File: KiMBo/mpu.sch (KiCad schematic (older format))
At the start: 11 parts, among them U1 OSD3358, U4 SN74AUC1G74DCTR

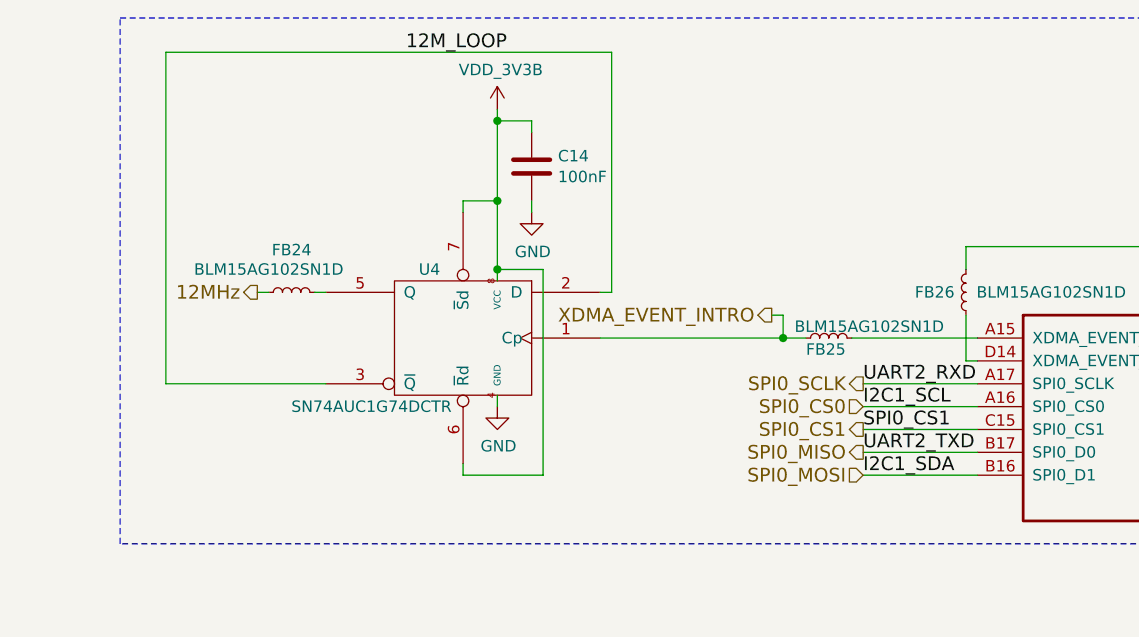
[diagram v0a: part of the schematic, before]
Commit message: Remove HDMI from the schematic
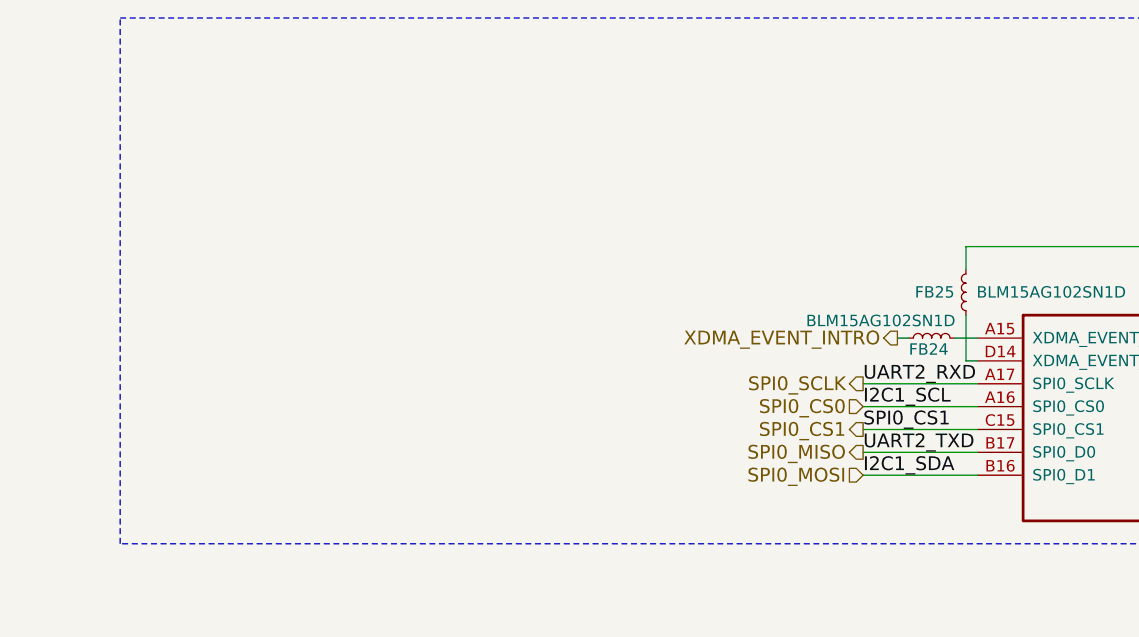
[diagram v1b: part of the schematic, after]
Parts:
- removed C14: 100nF, Capacitors_SMD:C_0603, symbol C
- removed FB24: BLM15AG102SN1D, Resistors_SMD:R_0402, symbol INDUCTOR_Small
- removed U4: SN74AUC1G74DCTR, KiMBo:DCT-MSOP-8_3x3mm_Pitch0.65mm, symbol 74LVC1G74
- renumbered FB25 to FB24, FB26 to FB25
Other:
- moved on the sheet: FB24
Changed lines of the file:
@@
 $Descr A3 16535 11693
 encoding utf-8
-Sheet 5 26
+Sheet 5 25
 Title ""
 Date ""
@@
 $EndComp
 $Comp
-L GND #PWR088
+L GND #PWR086
 U 1 1 584B7680
 P 6100 7850
-F 0 "#PWR088" H 6100 7600 50  0001 C CNN
+F 0 "#PWR086" H 6100 7600 50  0001 C CNN
 F 1 "GND" H 6105 7677 50  0000 C CNN
 F 2 "" H 6100 7850 50  0000 C CNN
@@
 	1    0    0    -1
 $EndComp
-$Comp
-L 74LVC1G74 U4
-U 1 1 584D5286
-P 6750 3850
-F 0 "U4" H 6850 4150 50  0000 L CNN
-F 1 "SN74AUC1G74DCTR" H 6800 3550 50  0000 L CNN
-F 2 "KiMBo:DCT-MSOP-8_3x3mm_Pitch0.65mm" H 6750 3850 50  0001 C CNN
-F 3 "" H 6750 3850 50  0000 C CNN
-	1    6750 3850
-	-1   0    0    -1
-$EndComp
-$Comp
-L GND #PWR089
-U 1 1 584D67FE
-P 6900 4150
-F 0 "#PWR089" H 6900 3900 50  0001 C CNN
-F 1 "GND" H 6905 3977 50  0000 C CNN
-F 2 "" H 6900 4150 50  0000 C CNN
-F 3 "" H 6900 4150 50  0000 C CNN
-	1    6900 4150
-	1    0    0    -1
-$EndComp
-$Comp
-L GND #PWR090
-U 1 1 584DD3A5
-P 7050 3300
-F 0 "#PWR090" H 7050 3050 50  0001 C CNN
-F 1 "GND" H 7055 3127 50  0000 C CNN
-F 2 "" H 7050 3300 50  0000 C CNN
-F 3 "" H 7050 3300 50  0000 C CNN
-	1    7050 3300
-	1    0    0    -1
-$EndComp
-Text Label 6500 2600 0    60   ~ 0
-12M_LOOP
 $Comp
 L R R28
@@
 	11150 3450 11150 3500
 Wire Wire Line
-	9000 3850 8450 3850
+	9000 3850 8900 3850
 Wire Wire Line
 	7200 6750 6750 6750
@@
 Wire Wire Line
 	7050 6450 7200 6450
-Wire Wire Line
-	7350 3850 8250 3850
-Wire Wire Line
-	6150 4050 5450 4050
-Wire Wire Line
-	5450 4050 5450 2600
-Wire Wire Line
-	5450 2600 7400 2600
-Wire Wire Line
-	7400 2600 7400 3650
-Wire Wire Line
-	7400 3650 7350 3650
-Wire Wire Line
-	6900 4150 6900 4100
-Wire Wire Line
-	6900 2850 6900 3600
-Wire Wire Line
-	6150 3650 6100 3650
-Wire Wire Line
-	5900 3650 5850 3650
-Wire Wire Line
-	6750 3300 6750 3250
-Wire Wire Line
-	6750 3250 6900 3250
-Connection ~ 6900 3250
-Wire Wire Line
-	6750 4450 7100 4450
-Wire Wire Line
-	7100 4450 7100 3550
-Wire Wire Line
-	7100 3550 6900 3550
-Connection ~ 6900 3550
-Wire Wire Line
-	7050 3300 7050 3250
-Wire Wire Line
-	7050 2950 7050 2900
-Wire Wire Line
-	7050 2900 6900 2900
-Connection ~ 6900 2900
 Wire Wire Line
 	9350 7550 9300 7550
@@
 Wire Notes Line
 	5250 4750 5250 2450
-Text HLabel 8100 3750 0    60   Output ~ 0
+Text HLabel 8650 3850 0    60   Output ~ 0
 XDMA_EVENT_INTRO
-Wire Wire Line
-	8150 3850 8150 3750
-Wire Wire Line
-	8150 3750 8100 3750
-Connection ~ 8150 3850
 Text HLabel 10300 3400 0    60   Output ~ 0
 CLKOUT2
@@
 SPI1_CS1
 $Comp
-L VDD_ADC #PWR091
+L VDD_ADC #PWR087
 U 1 1 59E85302
 P 7000 7650
-F 0 "#PWR091" H 7150 7600 50  0001 C CNN
+F 0 "#PWR087" H 7150 7600 50  0001 C CNN
 F 1 "VDD_ADC" H 7020 7793 50  0000 C CNN
 F 2 "" H 7000 7650 50  0000 C CNN
@@
 $EndComp
 $Comp
-L VDD_3V3B #PWR092
-U 1 1 59F9CAE6
-P 6900 2850
-F 0 "#PWR092" H 6900 2700 50  0001 C CNN
-F 1 "VDD_3V3B" H 6915 3023 50  0000 C CNN
-F 2 "" H 6900 2850 50  0000 C CNN
-F 3 "" H 6900 2850 50  0000 C CNN
-	1    6900 2850
-	1    0    0    -1
-$EndComp
-$Comp
-L VDD_3V3B #PWR093
+L VDD_3V3B #PWR088
 U 1 1 59FC1115
 P 6100 7050
-F 0 "#PWR093" H 6100 6900 50  0001 C CNN
+F 0 "#PWR088" H 6100 6900 50  0001 C CNN
 F 1 "VDD_3V3B" H 6115 7223 50  0000 C CNN
 F 2 "" H 6100 7050 50  0000 C CNN
@@
 $EndComp
 $Comp
-L GNDA #PWR094
+L GNDA #PWR089
 U 1 1 59FCC96D
 P 7050 6500
-F 0 "#PWR094" H 7050 6250 50  0001 C CNN
+F 0 "#PWR089" H 7050 6250 50  0001 C CNN
 F 1 "GNDA" H 7055 6327 50  0000 C CNN
 F 2 "" H 7050 6500 50  0000 C CNN
@@
 Internal 150Ω FB\nfrom E8 to VSS\nunused on Replicape
 $Comp
-L PWR_FLAG #FLG095
+L PWR_FLAG #FLG090
 U 1 1 59FD3D41
 P 7150 6400
-F 0 "#FLG095" H 7150 6495 50  0001 C CNN
+F 0 "#FLG090" H 7150 6495 50  0001 C CNN
 F 1 "PWR_FLAG" H 7150 6624 50  0000 C CNN
 F 2 "" H 7150 6400 50  0000 C CNN
@@
 	1    7150 6400
 	1    0    0    -1
-$EndComp
-$Comp
-L INDUCTOR_Small FB24
-U 1 1 5B034EFC
-P 6000 3650
-F 0 "FB24" V 6185 3650 50  0000 C CNN
-F 1 "BLM15AG102SN1D" V 6100 3750 50  0000 C CNN
-F 2 "Resistors_SMD:R_0402" H 6000 3650 50  0001 C CNN
-F 3 "" H 6000 3650 50  0000 C CNN
-	1    6000 3650
-	0    -1   -1   0
 $EndComp
 Text Notes 6450 8000 0    60   ~ 0
@@
 Wire Wire Line
 	8500 4050 9000 4050
-Text HLabel 5850 3650 0    60   Output ~ 0
-12MHz
-$Comp
-L INDUCTOR_Small FB26
+$Comp
+L INDUCTOR_Small FB25
 U 1 1 58CEF5B5
 P 8950 3650
-F 0 "FB26" H 9000 3650 50  0000 L CNN
+F 0 "FB25" H 9000 3650 50  0000 L CNN
 F 1 "BLM15AG102SN1D" H 8250 3650 50  0000 L CNN
 F 2 "Resistors_SMD:R_0402" H 8950 3650 50  0001 C CNN
@@
 $EndComp
 $Comp
-L INDUCTOR_Small FB25
+L INDUCTOR_Small FB24
 U 1 1 58CF0E6E
-P 8350 3850
-F 0 "FB25" V 8300 3750 50  0000 L CNN
-F 1 "BLM15AG102SN1D" V 8400 3700 50  0000 L CNN
-F 2 "Resistors_SMD:R_0402" H 8350 3850 50  0001 C CNN
-F 3 "" H 8350 3850 50  0000 C CNN
-	1    8350 3850
+P 8800 3850
+F 0 "FB24" V 8750 3750 50  0000 L CNN
+F 1 "BLM15AG102SN1D" V 8875 3300 50  0000 L CNN
+F 2 "Resistors_SMD:R_0402" H 8800 3850 50  0001 C CNN
+F 3 "" H 8800 3850 50  0000 C CNN
+	1    8800 3850
 	0    1    -1   0
-$EndComp
-$Comp
-L C C14
-U 1 1 58EAE0AA
-P 7050 3100
-F 0 "C14" H 7165 3146 50  0000 L CNN
-F 1 "100nF" H 7165 3055 50  0000 L CNN
-F 2 "Capacitors_SMD:C_0603" H 7088 2950 50  0001 C CNN
-F 3 "" H 7050 3100 50  0000 C CNN
-	1    7050 3100
-	1    0    0    -1
 $EndComp
 Text HLabel 8500 4350 0    60   Output ~ 0
@@
 SPI0_CS0
 Wire Wire Line
-	6750 4400 6750 4450
+	8650 3850 8700 3850
 $EndSCHEMATC

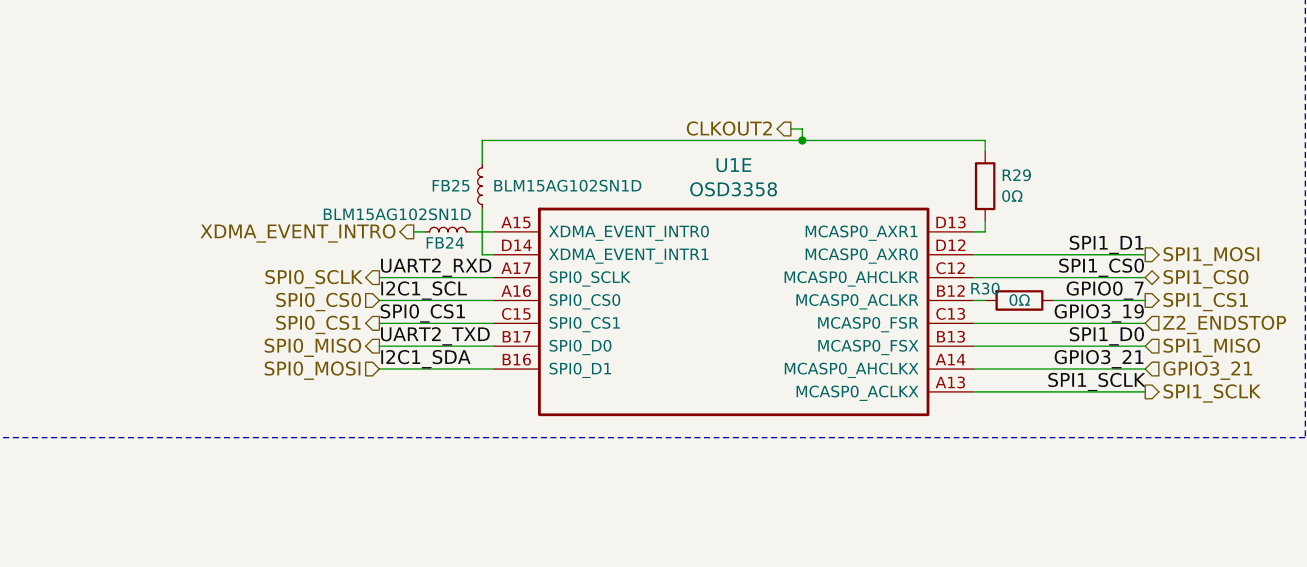
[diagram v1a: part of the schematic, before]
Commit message: Add F1 PTC resettable fuse at the 5V output, begin E's heater circuit layout
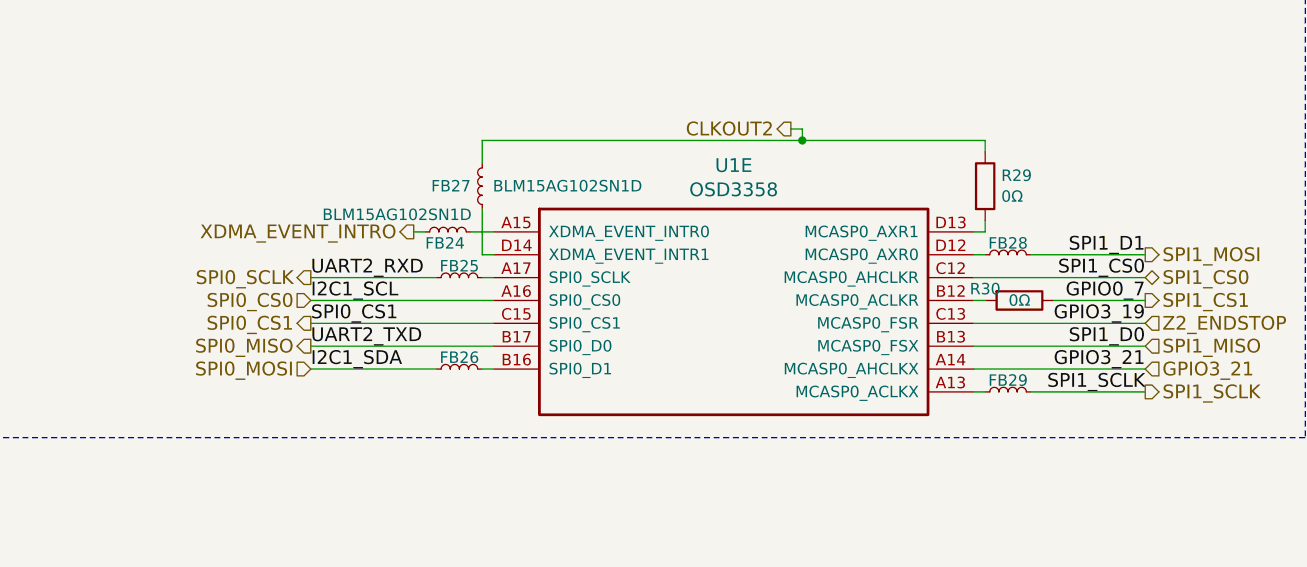
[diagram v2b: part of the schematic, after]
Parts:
- added FB25, FB26, FB28, FB29: MMZ1608A252BTA00, KiMBo:Ferrite_Bead_0603, symbol INDUCTOR_Small
- renumbered FB25 to FB27
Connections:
- net SPI0_MOSI: now also FB26.1; no longer U1.B16 (SPI0_D1)
- net SPI0_SCLK: now also FB25.1; no longer U1.A17 (SPI0_SCLK)
- net SPI1_MOSI: now also FB28.2; no longer U1.D12 (MCASP0_AXR0)
- net SPI1_SCLK: now also FB29.2; no longer U1.A13 (MCASP0_ACLKX)
- new net: FB29.1, U1.A13 (MCASP0_ACLKX)
- new net: FB25.2, U1.A17 (SPI0_SCLK)
- new net: FB26.2, U1.B16 (SPI0_D1)
- new net: FB28.1, U1.D12 (MCASP0_AXR0)
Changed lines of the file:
@@
 Text Notes 7450 6000 0    197  ~ 0
 Analog I/O
-Text Label 8500 4050 0    60   ~ 0
+Text Label 8200 4050 0    60   ~ 0
 UART2_RXD
-Text Label 8500 4350 0    60   ~ 0
+Text Label 8200 4350 0    60   ~ 0
 UART2_TXD
-Text Label 8500 4450 0    60   ~ 0
+Text Label 8200 4450 0    60   ~ 0
 I2C1_SDA
-Text Label 8500 4150 0    60   ~ 0
+Text Label 8200 4150 0    60   ~ 0
 I2C1_SCL
 $Comp
@@
 GPIO3_19
 Wire Wire Line
-	9000 4350 8500 4350
-Wire Wire Line
-	8500 4450 9000 4450
-Wire Wire Line
-	8500 4150 9000 4150
-Wire Wire Line
-	8500 4250 9000 4250
+	9000 4350 8200 4350
+Wire Wire Line
+	8200 4150 9000 4150
+Wire Wire Line
+	8200 4250 9000 4250
 Wire Wire Line
 	11100 3850 11150 3850
@@
 	11100 4450 11850 4450
 Wire Wire Line
-	11100 4550 11850 4550
-Wire Wire Line
 	11100 4350 11850 4350
 Wire Wire Line
 	11100 4250 11850 4250
-Wire Wire Line
-	11100 3950 11850 3950
 Wire Wire Line
 	11100 4050 11850 4050
@@
 Text Notes 2350 3450 0    197  ~ 0
 Unused
-Text HLabel 8500 4250 0    60   Output ~ 0
+Text HLabel 8200 4250 0    60   Output ~ 0
 SPI0_CS1
 Text HLabel 11850 4450 2    60   Input ~ 0
@@
 NoConn ~ 6750 7050
 NoConn ~ 6750 7250
-Text HLabel 8500 4050 0    60   Output ~ 0
+Text HLabel 8200 4050 0    60   Output ~ 0
 SPI0_SCLK
-Wire Wire Line
-	8500 4050 9000 4050
-$Comp
-L INDUCTOR_Small FB25
+$Comp
+L INDUCTOR_Small FB27
 U 1 1 58CEF5B5
 P 8950 3650
-F 0 "FB25" H 9000 3650 50  0000 L CNN
+F 0 "FB27" H 9000 3650 50  0000 L CNN
 F 1 "BLM15AG102SN1D" H 8250 3650 50  0000 L CNN
 F 2 "Resistors_SMD:R_0402" H 8950 3650 50  0001 C CNN
@@
 	0    1    -1   0
 $EndComp
-Text HLabel 8500 4350 0    60   Output ~ 0
+Text HLabel 8200 4350 0    60   Output ~ 0
 SPI0_MISO
-Text Label 8500 4250 0    60   ~ 0
+Text Label 8200 4250 0    60   ~ 0
 SPI0_CS1
-Text HLabel 8500 4450 0    60   Input ~ 0
+Text HLabel 8200 4450 0    60   Input ~ 0
 SPI0_MOSI
 Text HLabel 11850 4150 2    60   Output ~ 0
 SPI1_CS1
-Text HLabel 8500 4150 0    60   Input ~ 0
+Text HLabel 8200 4150 0    60   Input ~ 0
 SPI0_CS0
 Wire Wire Line
 	8650 3850 8700 3850
+$Comp
+L INDUCTOR_Small FB29
+U 1 1 59121B69
+P 11250 4550
+F 0 "FB29" V 11300 4550 50  0000 C CNN
+F 1 "MMZ1608A252BTA00" V 11200 4550 50  0001 C CNN
+F 2 "KiMBo:Ferrite_Bead_0603" H 11250 4550 50  0001 C CNN
+F 3 "" H 11250 4550 50  0000 C CNN
+	1    11250 4550
+	0    -1   -1   0
+$EndComp
+$Comp
+L INDUCTOR_Small FB28
+U 1 1 59121BDD
+P 11250 3950
+F 0 "FB28" V 11300 3950 50  0000 C CNN
+F 1 "MMZ1608A252BTA00" V 11200 3950 50  0001 C CNN
+F 2 "KiMBo:Ferrite_Bead_0603" H 11250 3950 50  0001 C CNN
+F 3 "" H 11250 3950 50  0000 C CNN
+	1    11250 3950
+	0    -1   -1   0
+$EndComp
+Wire Wire Line
+	11100 3950 11150 3950
+Wire Wire Line
+	11100 4550 11150 4550
+Wire Wire Line
+	11350 4550 11850 4550
+Wire Wire Line
+	11350 3950 11850 3950
+$Comp
+L INDUCTOR_Small FB25
+U 1 1 591407CC
+P 8850 4050
+F 0 "FB25" V 8900 4050 50  0000 C CNN
+F 1 "MMZ1608A252BTA00" V 8800 4050 50  0001 C CNN
+F 2 "KiMBo:Ferrite_Bead_0603" H 8850 4050 50  0001 C CNN
+F 3 "" H 8850 4050 50  0000 C CNN
+	1    8850 4050
+	0    -1   -1   0
+$EndComp
+$Comp
+L INDUCTOR_Small FB26
+U 1 1 59140942
+P 8850 4450
+F 0 "FB26" V 8900 4450 50  0000 C CNN
+F 1 "MMZ1608A252BTA00" V 8800 4450 50  0001 C CNN
+F 2 "KiMBo:Ferrite_Bead_0603" H 8850 4450 50  0001 C CNN
+F 3 "" H 8850 4450 50  0000 C CNN
+	1    8850 4450
+	0    -1   -1   0
+$EndComp
+Wire Wire Line
+	8200 4050 8750 4050
+Wire Wire Line
+	9000 4050 8950 4050
+Wire Wire Line
+	9000 4450 8950 4450
+Wire Wire Line
+	8750 4450 8200 4450
 $EndSCHEMATC

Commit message: Route 24V to the buck, add PTC fuse to 5V output
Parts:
- renumbered FB24 to FB33, FB25 to FB34, FB26 to FB35, FB27 to FB36, FB28 to FB37, FB29 to FB38
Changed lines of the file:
@@
 SPI0_SCLK
 $Comp
-L INDUCTOR_Small FB27
+L INDUCTOR_Small FB36
 U 1 1 58CEF5B5
 P 8950 3650
-F 0 "FB27" H 9000 3650 50  0000 L CNN
+F 0 "FB36" H 9000 3650 50  0000 L CNN
 F 1 "BLM15AG102SN1D" H 8250 3650 50  0000 L CNN
 F 2 "Resistors_SMD:R_0402" H 8950 3650 50  0001 C CNN
@@
 $EndComp
 $Comp
-L INDUCTOR_Small FB24
+L INDUCTOR_Small FB33
 U 1 1 58CF0E6E
 P 8800 3850
-F 0 "FB24" V 8750 3750 50  0000 L CNN
+F 0 "FB33" V 8750 3750 50  0000 L CNN
 F 1 "BLM15AG102SN1D" V 8875 3300 50  0000 L CNN
 F 2 "Resistors_SMD:R_0402" H 8800 3850 50  0001 C CNN
@@
 	8650 3850 8700 3850
 $Comp
-L INDUCTOR_Small FB29
+L INDUCTOR_Small FB38
 U 1 1 59121B69
 P 11250 4550
-F 0 "FB29" V 11300 4550 50  0000 C CNN
+F 0 "FB38" V 11300 4550 50  0000 C CNN
 F 1 "MMZ1608A252BTA00" V 11200 4550 50  0001 C CNN
 F 2 "KiMBo:Ferrite_Bead_0603" H 11250 4550 50  0001 C CNN
@@
 $EndComp
 $Comp
-L INDUCTOR_Small FB28
+L INDUCTOR_Small FB37
 U 1 1 59121BDD
 P 11250 3950
-F 0 "FB28" V 11300 3950 50  0000 C CNN
+F 0 "FB37" V 11300 3950 50  0000 C CNN
 F 1 "MMZ1608A252BTA00" V 11200 3950 50  0001 C CNN
 F 2 "KiMBo:Ferrite_Bead_0603" H 11250 3950 50  0001 C CNN
@@
 	11350 3950 11850 3950
 $Comp
-L INDUCTOR_Small FB25
+L INDUCTOR_Small FB34
 U 1 1 591407CC
 P 8850 4050
-F 0 "FB25" V 8900 4050 50  0000 C CNN
+F 0 "FB34" V 8900 4050 50  0000 C CNN
 F 1 "MMZ1608A252BTA00" V 8800 4050 50  0001 C CNN
 F 2 "KiMBo:Ferrite_Bead_0603" H 8850 4050 50  0001 C CNN
@@
 $EndComp
 $Comp
-L INDUCTOR_Small FB26
+L INDUCTOR_Small FB35
 U 1 1 59140942
 P 8850 4450
-F 0 "FB26" V 8900 4450 50  0000 C CNN
+F 0 "FB35" V 8900 4450 50  0000 C CNN
 F 1 "MMZ1608A252BTA00" V 8800 4450 50  0001 C CNN
 F 2 "KiMBo:Ferrite_Bead_0603" H 8850 4450 50  0001 C CNN

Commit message: Add ferrite beads to the 5V and 3V pins at the SPI connectors
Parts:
- renumbered FB33 to FB41, FB34 to FB42, FB35 to FB43, FB36 to FB44, FB37 to FB45, FB38 to FB46
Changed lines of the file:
@@
 $EndComp
 $Comp
-L GND #PWR086
+L GND #PWR083
 U 1 1 584B7680
 P 6100 7850
-F 0 "#PWR086" H 6100 7600 50  0001 C CNN
+F 0 "#PWR083" H 6100 7600 50  0001 C CNN
 F 1 "GND" H 6105 7677 50  0000 C CNN
 F 2 "" H 6100 7850 50  0000 C CNN
@@
 SPI1_CS1
 $Comp
-L VDD_ADC #PWR087
+L VDD_ADC #PWR084
 U 1 1 59E85302
 P 7000 7650
-F 0 "#PWR087" H 7150 7600 50  0001 C CNN
+F 0 "#PWR084" H 7150 7600 50  0001 C CNN
 F 1 "VDD_ADC" H 7020 7793 50  0000 C CNN
 F 2 "" H 7000 7650 50  0000 C CNN
@@
 $EndComp
 $Comp
-L VDD_3V3B #PWR088
+L VDD_3V3B #PWR085
 U 1 1 59FC1115
 P 6100 7050
-F 0 "#PWR088" H 6100 6900 50  0001 C CNN
+F 0 "#PWR085" H 6100 6900 50  0001 C CNN
 F 1 "VDD_3V3B" H 6115 7223 50  0000 C CNN
 F 2 "" H 6100 7050 50  0000 C CNN
@@
 $EndComp
 $Comp
-L GNDA #PWR089
+L GNDA #PWR086
 U 1 1 59FCC96D
 P 7050 6500
-F 0 "#PWR089" H 7050 6250 50  0001 C CNN
+F 0 "#PWR086" H 7050 6250 50  0001 C CNN
 F 1 "GNDA" H 7055 6327 50  0000 C CNN
 F 2 "" H 7050 6500 50  0000 C CNN
@@
 Internal 150Ω FB\nfrom E8 to VSS\nunused on Replicape
 $Comp
-L PWR_FLAG #FLG090
+L PWR_FLAG #FLG087
 U 1 1 59FD3D41
 P 7150 6400
-F 0 "#FLG090" H 7150 6495 50  0001 C CNN
+F 0 "#FLG087" H 7150 6495 50  0001 C CNN
 F 1 "PWR_FLAG" H 7150 6624 50  0000 C CNN
 F 2 "" H 7150 6400 50  0000 C CNN
@@
 SPI0_SCLK
 $Comp
-L INDUCTOR_Small FB36
+L INDUCTOR_Small FB44
 U 1 1 58CEF5B5
 P 8950 3650
-F 0 "FB36" H 9000 3650 50  0000 L CNN
+F 0 "FB44" H 9000 3650 50  0000 L CNN
 F 1 "BLM15AG102SN1D" H 8250 3650 50  0000 L CNN
 F 2 "Resistors_SMD:R_0402" H 8950 3650 50  0001 C CNN
@@
 $EndComp
 $Comp
-L INDUCTOR_Small FB33
+L INDUCTOR_Small FB41
 U 1 1 58CF0E6E
 P 8800 3850
-F 0 "FB33" V 8750 3750 50  0000 L CNN
+F 0 "FB41" V 8750 3750 50  0000 L CNN
 F 1 "BLM15AG102SN1D" V 8875 3300 50  0000 L CNN
 F 2 "Resistors_SMD:R_0402" H 8800 3850 50  0001 C CNN
@@
 	8650 3850 8700 3850
 $Comp
-L INDUCTOR_Small FB38
+L INDUCTOR_Small FB46
 U 1 1 59121B69
 P 11250 4550
-F 0 "FB38" V 11300 4550 50  0000 C CNN
+F 0 "FB46" V 11300 4550 50  0000 C CNN
 F 1 "MMZ1608A252BTA00" V 11200 4550 50  0001 C CNN
 F 2 "KiMBo:Ferrite_Bead_0603" H 11250 4550 50  0001 C CNN
@@
 $EndComp
 $Comp
-L INDUCTOR_Small FB37
+L INDUCTOR_Small FB45
 U 1 1 59121BDD
 P 11250 3950
-F 0 "FB37" V 11300 3950 50  0000 C CNN
+F 0 "FB45" V 11300 3950 50  0000 C CNN
 F 1 "MMZ1608A252BTA00" V 11200 3950 50  0001 C CNN
 F 2 "KiMBo:Ferrite_Bead_0603" H 11250 3950 50  0001 C CNN
@@
 	11350 3950 11850 3950
 $Comp
-L INDUCTOR_Small FB34
+L INDUCTOR_Small FB42
 U 1 1 591407CC
 P 8850 4050
-F 0 "FB34" V 8900 4050 50  0000 C CNN
+F 0 "FB42" V 8900 4050 50  0000 C CNN
 F 1 "MMZ1608A252BTA00" V 8800 4050 50  0001 C CNN
 F 2 "KiMBo:Ferrite_Bead_0603" H 8850 4050 50  0001 C CNN
@@
 $EndComp
 $Comp
-L INDUCTOR_Small FB35
+L INDUCTOR_Small FB43
 U 1 1 59140942
 P 8850 4450
-F 0 "FB35" V 8900 4450 50  0000 C CNN
+F 0 "FB43" V 8900 4450 50  0000 C CNN
 F 1 "MMZ1608A252BTA00" V 8800 4450 50  0001 C CNN
 F 2 "KiMBo:Ferrite_Bead_0603" H 8850 4450 50  0001 C CNN
